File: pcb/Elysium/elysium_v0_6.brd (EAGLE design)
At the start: 160 x 114 mm, 20 parts, among them U1 TLC5940-NT, U2 TLC5940-NT, U3 TLC5940-NT, U4 TLC5940-NT, X1 5566-20

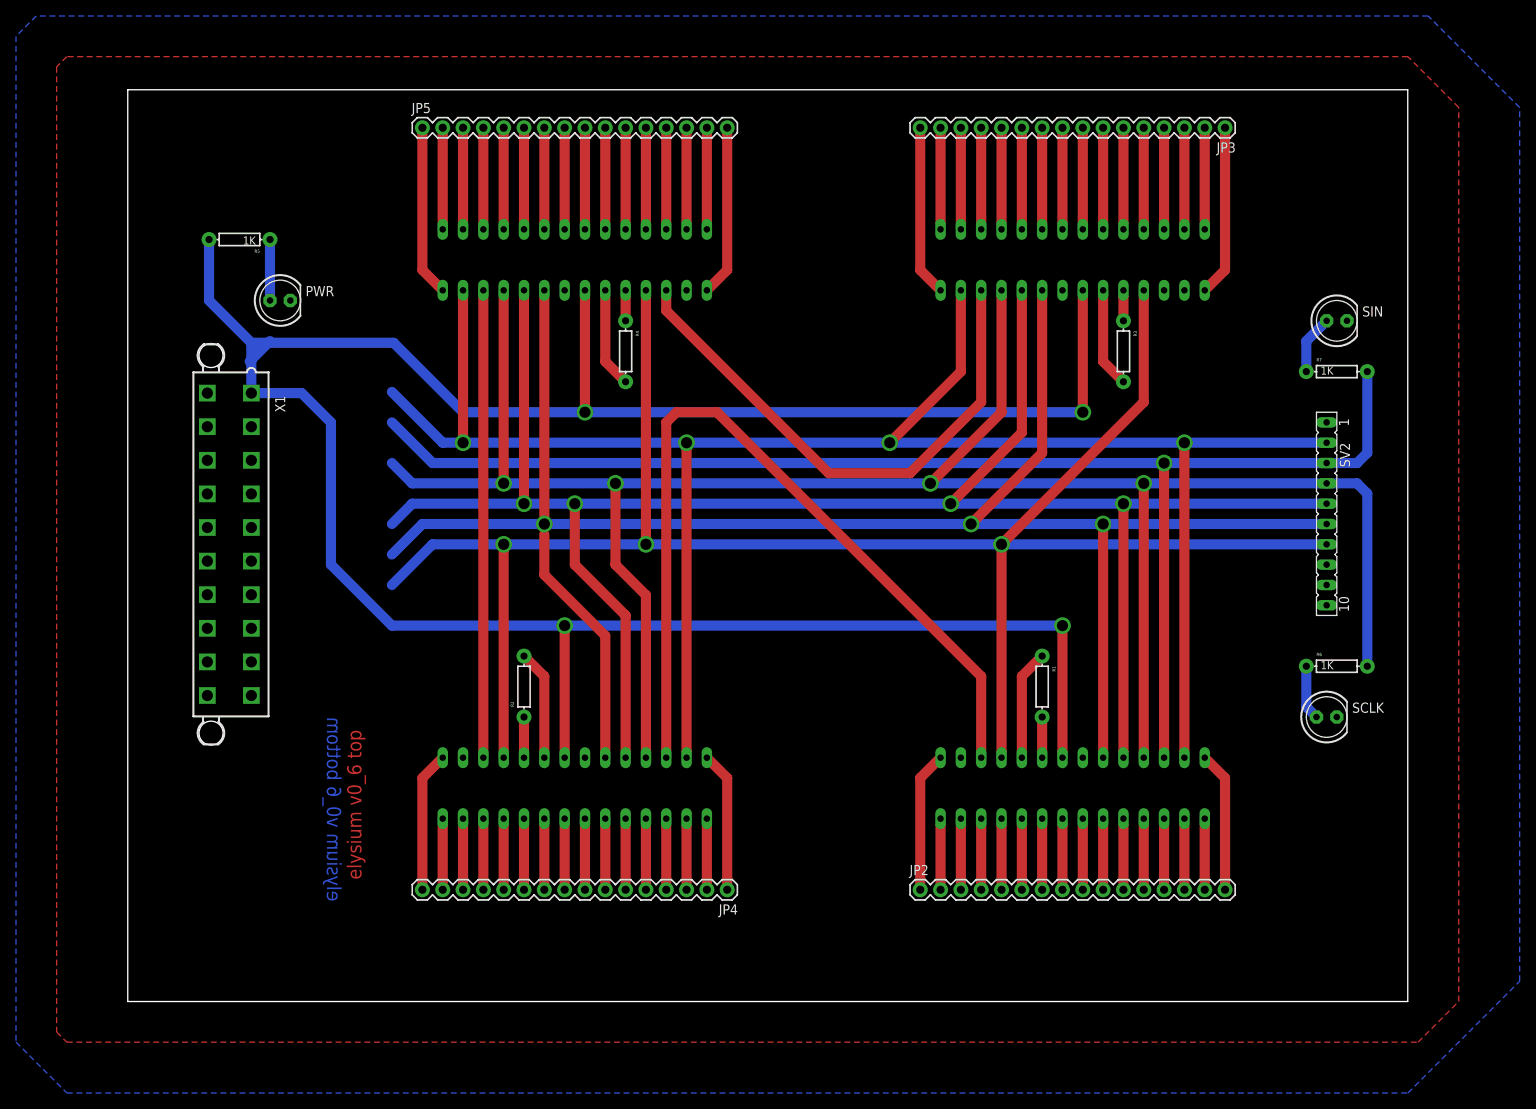
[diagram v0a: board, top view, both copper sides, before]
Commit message: Added mounting holes to v0.6 PCB.
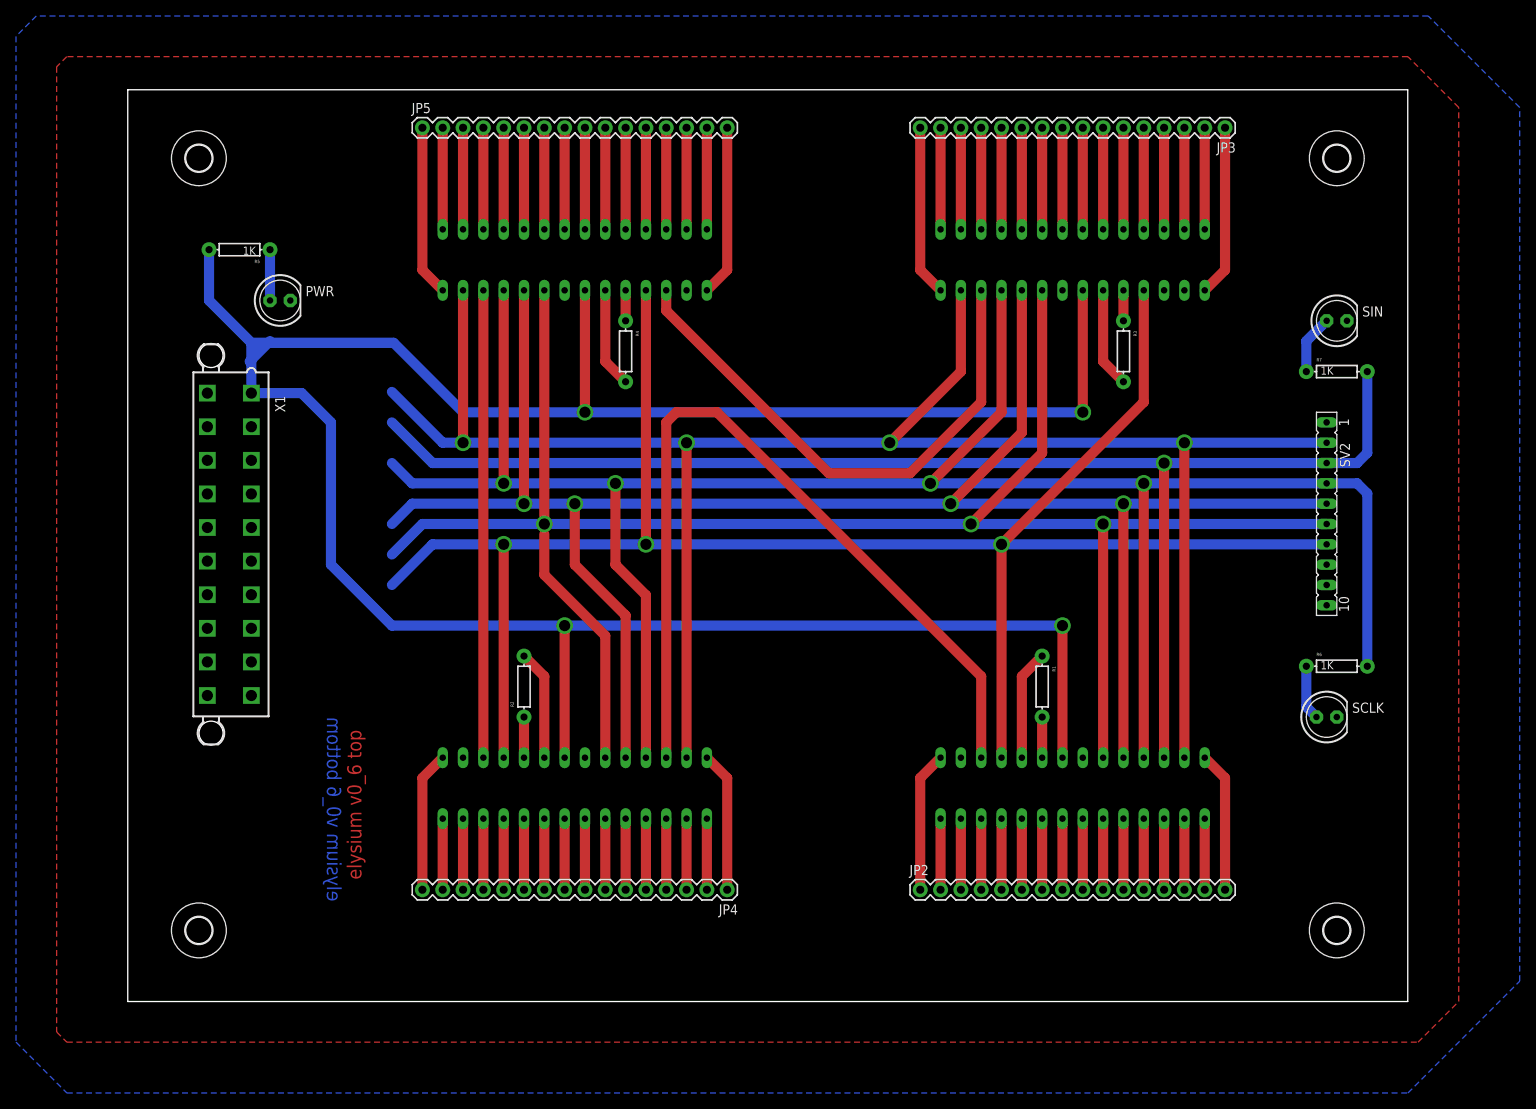
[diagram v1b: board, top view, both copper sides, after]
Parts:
- added H1, H2, H3, H4: MOUNT-HOLE3.3, holes:3,3
- moved R5 1.27 mm to (14.0, 85.1)
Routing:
- net N$69: track 7.62 -> 6.35 mm
- net VCC: track 316.3 -> 315.0 mm
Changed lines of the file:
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@@
 <element name="R4" library="SparkFun-Resistors" package="AXIAL-0.3EZ" value="" x="62.23" y="72.39" rot="R270"/>
 <element name="PWR" library="adafruit" package="LED5MM" value="" x="19.05" y="78.74"/>
-<element name="R5" library="SparkFun-Resistors" package="AXIAL-0.3EZ" value="1K" x="13.97" y="86.36" rot="R180"/>
+<element name="R5" library="SparkFun-Resistors" package="AXIAL-0.3EZ" value="1K" x="13.97" y="85.09" rot="R180"/>
 <element name="SCLK" library="adafruit" package="LED5MM" value="" x="149.86" y="26.67"/>
 <element name="R6" library="SparkFun-Resistors" package="AXIAL-0.3EZ" value="1K" x="151.13" y="33.02"/>
@@
 <attribute name="OC_FARNELL" value="unknown" x="44.45" y="15.24" size="1.778" layer="27" rot="R270" display="off"/>
 </element>
+<element name="H1" library="holes" package="3,3" value="MOUNT-HOLE3.3" x="8.89" y="96.52"/>
+<element name="H2" library="holes" package="3,3" value="MOUNT-HOLE3.3" x="8.89" y="0"/>
+<element name="H3" library="holes" package="3,3" value="MOUNT-HOLE3.3" x="151.13" y="96.52"/>
+<element name="H4" library="holes" package="3,3" value="MOUNT-HOLE3.3" x="151.13" y="0"/>
 </elements>
 <signals>
@@
 <wire x1="15.45" y1="67.16" x2="15.45" y2="73.45" width="1.27" layer="16"/>
 <wire x1="15.45" y1="73.45" x2="10.16" y2="78.74" width="1.27" layer="16"/>
-<wire x1="10.16" y1="78.74" x2="10.16" y2="86.36" width="1.27" layer="16"/>
+<wire x1="10.16" y1="78.74" x2="10.16" y2="85.09" width="1.27" layer="16"/>
 <wire x1="15.45" y1="73.45" x2="33.23" y2="73.45" width="1.27" layer="16"/>
 <wire x1="33.23" y1="73.45" x2="41.91" y2="64.77" width="1.27" layer="16"/>
@@
 <contactref element="R5" pad="P$1"/>
 <contactref element="PWR" pad="A"/>
-<wire x1="17.78" y1="86.36" x2="17.78" y2="78.74" width="1.27" layer="16"/>
+<wire x1="17.78" y1="85.09" x2="17.78" y2="78.74" width="1.27" layer="16"/>
 </signal>
 <signal name="N$74">
